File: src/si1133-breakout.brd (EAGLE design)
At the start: 18 x 8 mm, 6 parts, among them J1 PTH VERT MALE, J2 PTH VERT MALE, U1 SI1133-AA00-GMR

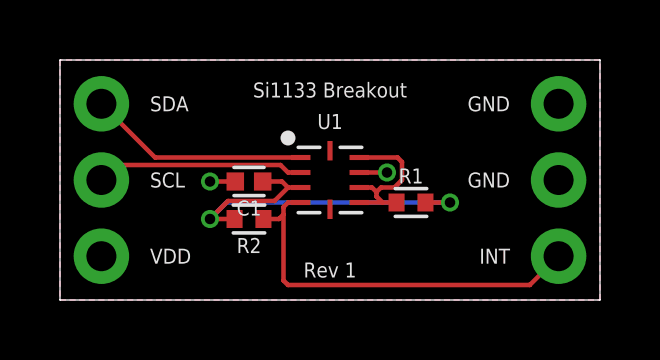
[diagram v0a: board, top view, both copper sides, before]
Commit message: Update to fit OSH Park 2-layer DRU.
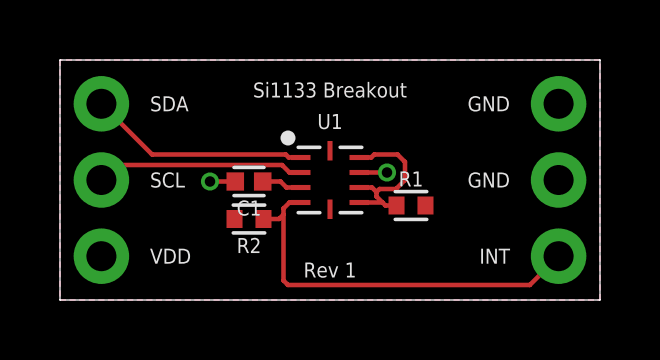
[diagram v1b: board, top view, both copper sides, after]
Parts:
- moved R1 0.10 mm to (2.70, -0.85)
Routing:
- net VDD: track 14.2 -> 1.35 mm, vias 2 -> 0
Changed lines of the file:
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@@
 <setting verticaltext="up"/>
 </settings>
-<grid distance="1" unitdist="mm" unit="mm" style="lines" multiple="1" display="yes" altdistance="0.1" altunitdist="mm" altunit="mm"/>
+<grid distance="0.1" unitdist="mm" unit="mm" style="lines" multiple="1" display="yes" altdistance="0.05" altunitdist="mm" altunit="mm"/>
 <layers>
 <layer number="1" name="Top" color="4" fill="1" visible="yes" active="yes"/>
@@
 </class>
 </classes>
-<designrules name="stella-wearables">
-<description language="en">&lt;b&gt;Stella Wearables Design Rules based on OSH Park Design Rules&lt;/b&gt;
+<designrules name="oshpark-2layer">
+<description language="en">&lt;b&gt;OSH Park Design Rules&lt;/b&gt;
 &lt;p&gt;
 Please make sure your boards conform to these design rules.
@@
 <param name="mtCopper" value="0.035559375mm 0.0356mm 0.0356mm 0.0356mm 0.0356mm 0.0356mm 0.0356mm 0.0356mm 0.0356mm 0.0356mm 0.0356mm 0.0356mm 0.0356mm 0.0356mm 0.0356mm 0.035559375mm"/>
 <param name="mtIsolate" value="1.6mm 0.1499mm 0.2007mm 0.1499mm 0.2007mm 0.1499mm 0.2007mm 0.1499mm 0.2007mm 0.1499mm 0.2007mm 0.1499mm 0.2007mm 0.1499mm 0.2007mm"/>
-<param name="mdWireWire" value="3mil"/>
-<param name="mdWirePad" value="3mil"/>
-<param name="mdWireVia" value="3mil"/>
-<param name="mdPadPad" value="3mil"/>
-<param name="mdPadVia" value="3mil"/>
-<param name="mdViaVia" value="3mil"/>
-<param name="mdSmdPad" value="3mil"/>
-<param name="mdSmdVia" value="3mil"/>
-<param name="mdSmdSmd" value="3mil"/>
+<param name="mdWireWire" value="6mil"/>
+<param name="mdWirePad" value="6mil"/>
+<param name="mdWireVia" value="6mil"/>
+<param name="mdPadPad" value="6mil"/>
+<param name="mdPadVia" value="6mil"/>
+<param name="mdViaVia" value="6mil"/>
+<param name="mdSmdPad" value="6mil"/>
+<param name="mdSmdVia" value="6mil"/>
+<param name="mdSmdSmd" value="6mil"/>
 <param name="mdViaViaSameLayer" value="8mil"/>
 <param name="mnLayersViaInSmd" value="2"/>
@@
 <param name="mdDrill" value="6mil"/>
 <param name="mdSmdStop" value="0mil"/>
-<param name="msWidth" value="3mil"/>
-<param name="msDrill" value="6mil"/>
+<param name="msWidth" value="6mil"/>
+<param name="msDrill" value="10mil"/>
 <param name="msMicroVia" value="10mil"/>
 <param name="msBlindViaRatio" value="0.5"/>
@@
 <attribute name="VALUE" x="-2.7" y="0.585" size="0.25" layer="27" font="vector" ratio="10" rot="R180" align="top-center"/>
 </element>
-<element name="R1" library="_resistors" package="RESC1005X35_SMD-0402" package3d_urn="urn:adsk.eagle:package:2899165/1" value="10K" x="2.7" y="-0.75" smashed="yes">
-<attribute name="DATASHEET" value="http://www.yageo.com/NewPortal/yageodocoutput?fileName=/pdf/R-Chip/PYu-RC_51_RoHS_P_0.pdf" x="-1.11" y="1.79" size="1.778" layer="27" display="off"/>
-<attribute name="DIST" value="Digikey" x="-1.11" y="1.79" size="1.778" layer="27" display="off"/>
-<attribute name="DISTLINK" value="https://www.digikey.com/products/en?keywords=YAG1281CT-ND" x="-1.11" y="1.79" size="1.778" layer="27" display="off"/>
-<attribute name="DISTPN" value="YAG1281CT-ND" x="-1.11" y="1.79" size="1.778" layer="27" display="off"/>
-<attribute name="MFR" value="Yageo" x="-1.11" y="1.79" size="1.778" layer="27" display="off"/>
-<attribute name="MPN" value="RC0402JR-0710KP" x="-1.11" y="1.79" size="1.778" layer="27" display="off"/>
-<attribute name="NAME" x="2.7" y="-0.115" size="0.5" layer="25" font="vector" ratio="10" align="bottom-center"/>
-<attribute name="VALUE" x="2.7" y="-1.385" size="0.25" layer="27" font="vector" ratio="10" align="top-center"/>
+<element name="R1" library="_resistors" package="RESC1005X35_SMD-0402" package3d_urn="urn:adsk.eagle:package:2899165/1" value="10K" x="2.7" y="-0.85" smashed="yes">
+<attribute name="DATASHEET" value="http://www.yageo.com/NewPortal/yageodocoutput?fileName=/pdf/R-Chip/PYu-RC_51_RoHS_P_0.pdf" x="-1.11" y="1.69" size="1.778" layer="27" display="off"/>
+<attribute name="DIST" value="Digikey" x="-1.11" y="1.69" size="1.778" layer="27" display="off"/>
+<attribute name="DISTLINK" value="https://www.digikey.com/products/en?keywords=YAG1281CT-ND" x="-1.11" y="1.69" size="1.778" layer="27" display="off"/>
+<attribute name="DISTPN" value="YAG1281CT-ND" x="-1.11" y="1.69" size="1.778" layer="27" display="off"/>
+<attribute name="MFR" value="Yageo" x="-1.11" y="1.69" size="1.778" layer="27" display="off"/>
+<attribute name="MPN" value="RC0402JR-0710KP" x="-1.11" y="1.69" size="1.778" layer="27" display="off"/>
+<attribute name="NAME" x="2.7" y="-0.215" size="0.5" layer="25" font="vector" ratio="10" align="bottom-center"/>
+<attribute name="VALUE" x="2.7" y="-1.485" size="0.25" layer="27" font="vector" ratio="10" align="top-center"/>
 </element>
 <element name="J1" library="_connectors" package="HDRV3W64P254_1X3_762X254X838B" package3d_urn="urn:adsk.eagle:package:25811449/1" value="PTH VERT MALE" x="-7.62" y="0" smashed="yes" rot="MR270">
@@
 <signal name="SCL">
 <contactref element="U1" pad="2"/>
-<wire x1="-0.975" y1="0.25" x2="-1.4" y2="0.25" width="0.1524" layer="1"/>
-<wire x1="-1.65" y1="0.5" x2="-1.4" y2="0.25" width="0.1524" layer="1"/>
+<wire x1="-0.975" y1="0.25" x2="-1.35" y2="0.25" width="0.1524" layer="1"/>
+<wire x1="-1.6" y1="0.5" x2="-1.35" y2="0.25" width="0.1524" layer="1"/>
 <contactref element="J1" pad="2"/>
 <wire x1="-7.62" y1="0" x2="-7.12" y2="0.5" width="0.1524" layer="1"/>
-<wire x1="-7.12" y1="0.5" x2="-1.65" y2="0.5" width="0.1524" layer="1"/>
+<wire x1="-7.12" y1="0.5" x2="-1.6" y2="0.5" width="0.1524" layer="1"/>
 </signal>
 <signal name="SDA">
 <contactref element="U1" pad="1"/>
 <contactref element="J1" pad="1"/>
-<wire x1="-7.62" y1="2.54" x2="-5.83" y2="0.75" width="0.1524" layer="1"/>
-<wire x1="-5.83" y1="0.75" x2="-0.975" y2="0.75" width="0.1524" layer="1"/>
+<wire x1="-7.62" y1="2.54" x2="-5.93" y2="0.85" width="0.1524" layer="1"/>
+<wire x1="-1.475" y1="0.85" x2="-5.93" y2="0.85" width="0.1524" layer="1"/>
+<wire x1="-1.375" y1="0.75" x2="-0.975" y2="0.75" width="0.1524" layer="1"/>
+<wire x1="-1.375" y1="0.75" x2="-1.475" y2="0.85" width="0.1524" layer="1"/>
 </signal>
 <signal name="VDD">
@@
 <contactref element="C1" pad="1"/>
 <contactref element="R2" pad="2"/>
-<wire x1="-0.975" y1="-0.25" x2="-1.4" y2="-0.25" width="0.1524" layer="1"/>
-<wire x1="-2.2425" y1="-0.05" x2="-1.6" y2="-0.05" width="0.1524" layer="1"/>
-<wire x1="-1.6" y1="-0.05" x2="-1.4" y2="-0.25" width="0.1524" layer="1"/>
-<via x="-4" y="-1.3" extent="1-16" drill="0.35" diameter="0.1524"/>
-<wire x1="-3.1825" y1="-1.3" x2="-4" y2="-1.3" width="0.1524" layer="1"/>
-<wire x1="-3.4" y1="-0.7" x2="-4" y2="-1.3" width="0.1524" layer="1"/>
-<wire x1="-1.4" y1="-0.25" x2="-1.85" y2="-0.7" width="0.1524" layer="1"/>
-<wire x1="-1.85" y1="-0.7" x2="-3.4" y2="-0.7" width="0.1524" layer="1"/>
-<via x="4" y="-0.75" extent="1-16" drill="0.35" diameter="0.1524"/>
-<wire x1="3.1825" y1="-0.75" x2="4" y2="-0.75" width="0.1524" layer="1"/>
-<wire x1="4" y1="-0.75" x2="-3.45" y2="-0.75" width="0.1524" layer="16"/>
-<wire x1="-3.45" y1="-0.75" x2="-4" y2="-1.3" width="0.1524" layer="16"/>
 <contactref element="J1" pad="3"/>
 <polygon width="0.1524" layer="1">
@@
 <vertex x="-9" y="4"/>
 </polygon>
+<wire x1="-1.45" y1="-0.25" x2="-0.975" y2="-0.25" width="0.1524" layer="1"/>
+<wire x1="-2.2425" y1="-0.05" x2="-1.65" y2="-0.05" width="0.1524" layer="1"/>
+<wire x1="-1.65" y1="-0.05" x2="-1.45" y2="-0.25" width="0.1524" layer="1"/>
 </signal>
 <signal name="N$1">
@@
 <contactref element="U1" pad="7"/>
 <contactref element="U1" pad="6"/>
-<wire x1="0.975" y1="0.75" x2="2.25" y2="0.75" width="0.1524" layer="1"/>
-<wire x1="2.25" y1="0.75" x2="2.4" y2="0.6" width="0.1524" layer="1"/>
-<wire x1="2.4" y1="0.6" x2="2.4" y2="0" width="0.1524" layer="1"/>
-<wire x1="2.4" y1="0" x2="2.15" y2="-0.25" width="0.1524" layer="1"/>
+<wire x1="1.475" y1="0.85" x2="1.375" y2="0.75" width="0.1524" layer="1"/>
+<wire x1="0.975" y1="0.75" x2="1.375" y2="0.75" width="0.1524" layer="1"/>
+<wire x1="2.25" y1="0.85" x2="1.475" y2="0.85" width="0.1524" layer="1"/>
+<wire x1="2.25" y1="0.85" x2="2.5" y2="0.6" width="0.1524" layer="1"/>
+<wire x1="2.5" y1="0.6" x2="2.5" y2="0" width="0.1524" layer="1"/>
+<wire x1="2.5" y1="0" x2="2.2" y2="-0.3" width="0.1524" layer="1"/>
 <wire x1="0.975" y1="-0.25" x2="1.4" y2="-0.25" width="0.1524" layer="1"/>
 <wire x1="1.4" y1="-0.25" x2="1.55" y2="-0.4" width="0.1524" layer="1"/>
 <wire x1="1.55" y1="-0.4" x2="1.55" y2="-0.55" width="0.1524" layer="1"/>
 <wire x1="1.55" y1="-0.55" x2="1.75" y2="-0.75" width="0.1524" layer="1"/>
-<wire x1="1.75" y1="-0.75" x2="2.2175" y2="-0.75" width="0.1524" layer="1"/>
+<wire x1="1.75" y1="-0.75" x2="1.85" y2="-0.85" width="0.1524" layer="1"/>
+<wire x1="1.85" y1="-0.85" x2="2.2175" y2="-0.85" width="0.1524" layer="1"/>
 <wire x1="0.975" y1="-0.75" x2="1.75" y2="-0.75" width="0.1524" layer="1"/>
-<wire x1="1.7" y1="-0.25" x2="1.55" y2="-0.4" width="0.1524" layer="1"/>
-<wire x1="2.15" y1="-0.25" x2="1.7" y2="-0.25" width="0.1524" layer="1"/>
+<wire x1="1.65" y1="-0.3" x2="1.55" y2="-0.4" width="0.1524" layer="1"/>
+<wire x1="2.2" y1="-0.3" x2="1.65" y2="-0.3" width="0.1524" layer="1"/>
 </signal>
 <signal name="INT">
 <contactref element="U1" pad="4"/>
 <contactref element="R2" pad="1"/>
-<wire x1="-0.975" y1="-0.75" x2="-1.4" y2="-0.75" width="0.1524" layer="1"/>
-<wire x1="-1.4" y1="-0.75" x2="-1.55" y2="-0.9" width="0.1524" layer="1"/>
+<wire x1="-0.975" y1="-0.75" x2="-1.35" y2="-0.75" width="0.1524" layer="1"/>
+<wire x1="-1.35" y1="-0.75" x2="-1.55" y2="-0.95" width="0.1524" layer="1"/>
 <wire x1="-2.2175" y1="-1.3" x2="-1.7" y2="-1.3" width="0.1524" layer="1"/>
-<wire x1="-1.55" y1="-0.9" x2="-1.55" y2="-1.15" width="0.1524" layer="1"/>
+<wire x1="-1.55" y1="-0.95" x2="-1.55" y2="-1.15" width="0.1524" layer="1"/>
 <wire x1="-1.7" y1="-1.3" x2="-1.55" y2="-1.15" width="0.1524" layer="1"/>
 <contactref element="J2" pad="3"/>
